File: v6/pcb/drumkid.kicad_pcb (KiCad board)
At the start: 2 copper layers, 90 x 140 mm, 52 parts, among them J1 DIN-5_180degree, J2 DIN-5_180degree, J3 Conn_01x15, J4 Conn_01x15, J9 AudioJack3_Ground_Switch, SW1 SW_Push, SW2 SW_Push, SW3 SW_Push, SW4 SW_Push, SW5 SW_Push, SW6 SW_Push, SW7 SW_SPDT, SW8 SW_SPDT, U1 6N138

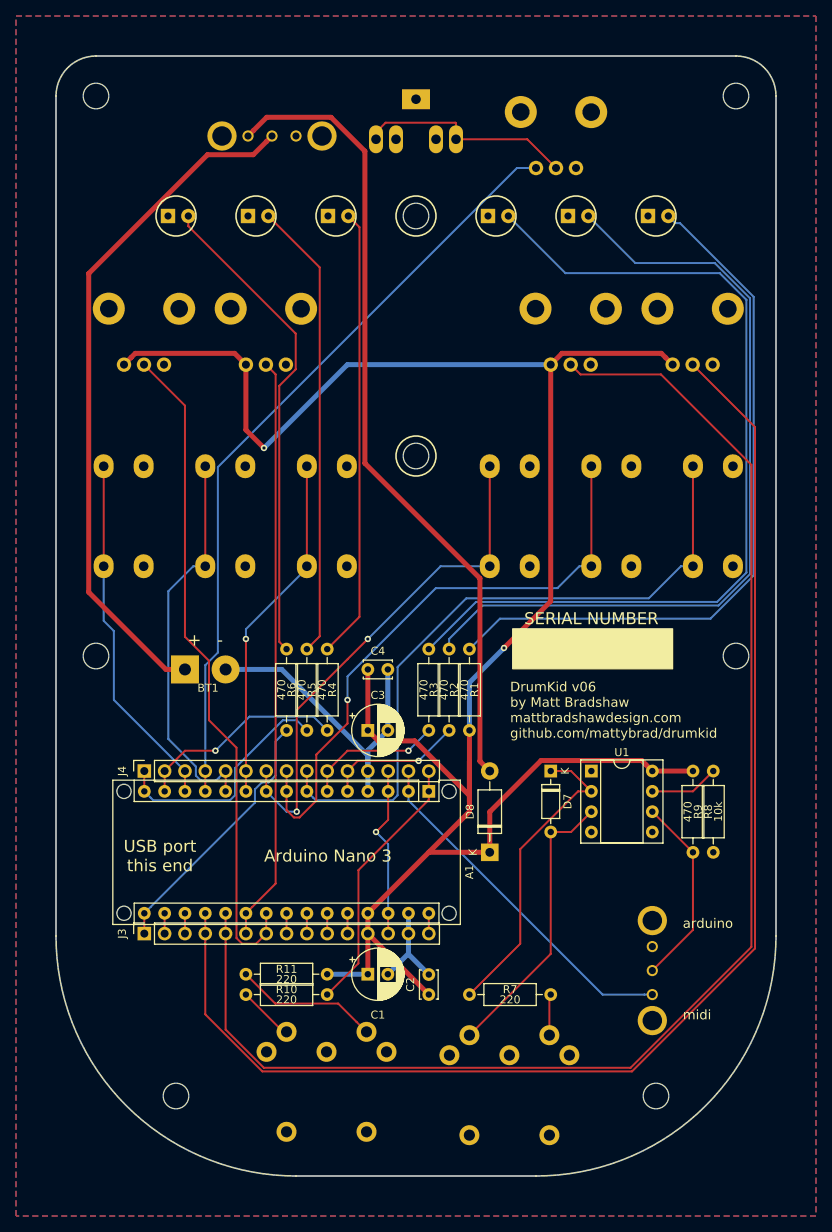
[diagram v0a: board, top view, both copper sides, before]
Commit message: added mounting holes
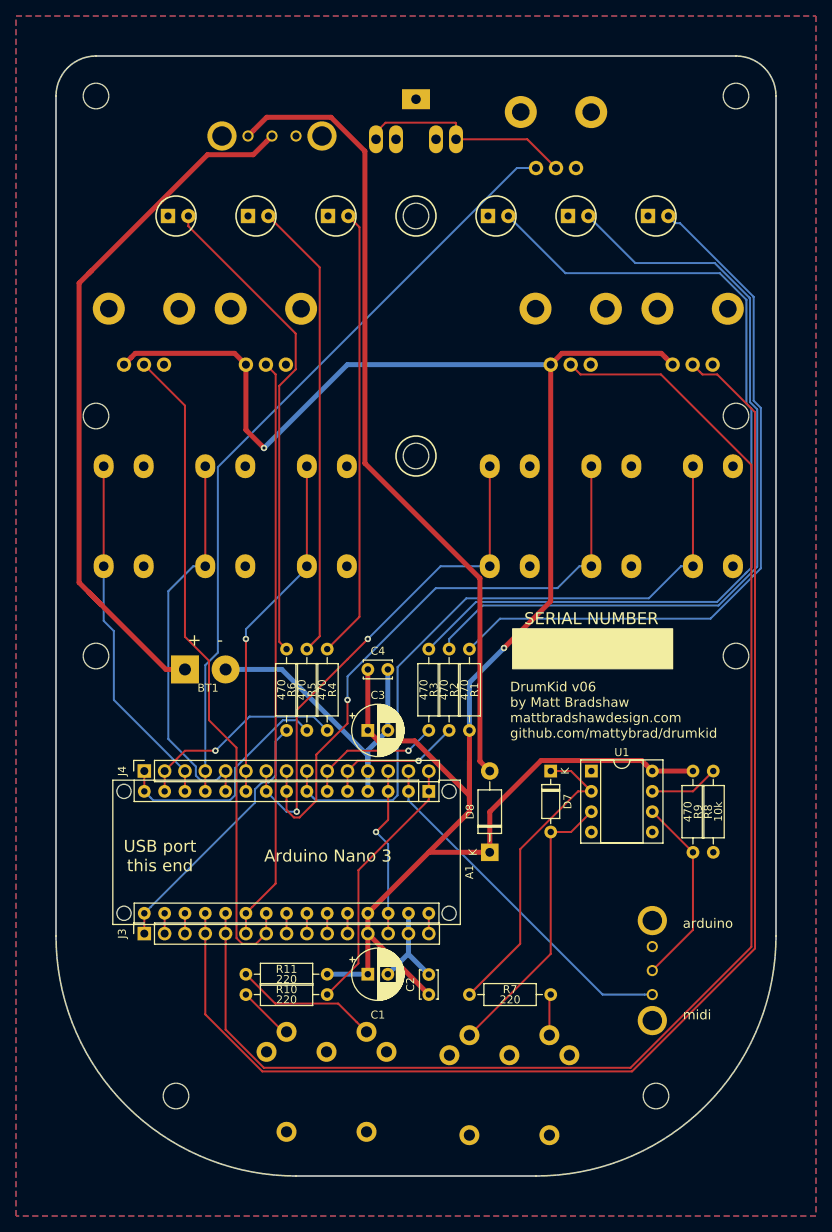
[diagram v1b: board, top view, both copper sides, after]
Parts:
- added H10: MountingHole, drumkidcustom:MountingHole_3.2mm_M3, B.Cu at (140.0, 75.0)
- added H9: MountingHole, drumkidcustom:MountingHole_3.2mm_M3, B.Cu at (60.0, 75.0)
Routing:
- net Net-(BT1-Pad1): track 85.9 -> 89.5 mm
- net /ANALOG_0: track 166.9 -> 168.0 mm
- net Net-(D2-Pad2): track 101.2 -> 102.1 mm
- net Net-(D1-Pad2): track 89.0 -> 89.8 mm
- net Net-(D3-Pad2): track 111.9 -> 112.5 mm
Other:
- board text added: "chance pitch note beat"
- board text added: "midpoint drop drone gremlin"
- board text added: "range crop modulate beats/bar"
- board text added: "zoom crush tuning tempo"
- board text removed: "chance pitch slop beat"

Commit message: finalised parameter labels on pcb
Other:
- board text added: "chance pitch drone beat"
- board text added: "midpoint drop note tempo"
- board text added: "range crop tuning swing"
- board text added: "zoom crush modulate beats/bar"
- board text removed: "chance pitch note beat"
- board text removed: "midpoint drop drone gremlin"
- board text removed: "range crop modulate beats/bar"
- board text removed: "zoom crush tuning tempo"
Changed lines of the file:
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@@
   (gr_line (start 144.9324 71.1708) (end 54.991 71.1708) (layer B.SilkS) (width 0.1))
   (gr_line (start 144.9324 73.279) (end 54.9656 73.279) (layer B.SilkS) (width 0.1))
-  (gr_text "midpoint\ndrop\ndrone\ngremlin" (at 66.04 73.66) (layer B.SilkS)
+  (gr_text "midpoint\ndrop\nnote\ntempo" (at 66.04 73.66) (layer B.SilkS)
     (effects (font (size 1.2 1.2) (thickness 0.3)) (justify mirror))
   )
-  (gr_text "range\ncrop\nmodulate\nbeats/bar" (at 81.28 73.66) (layer B.SilkS)
+  (gr_text "range\ncrop\ntuning\nswing" (at 81.28 73.66) (layer B.SilkS)
     (effects (font (size 1.2 1.2) (thickness 0.3)) (justify mirror))
   )
-  (gr_text "zoom\ncrush\ntuning\ntempo" (at 119.38 73.66) (layer B.SilkS)
+  (gr_text "zoom\ncrush\nmodulate\nbeats/bar" (at 119.38 73.66) (layer B.SilkS)
     (effects (font (size 1.2 1.2) (thickness 0.3)) (justify mirror))
   )
-  (gr_text "chance\npitch\nnote\nbeat" (at 134.62 73.66) (layer B.SilkS)
+  (gr_text "chance\npitch\ndrone\nbeat" (at 134.62 73.66) (layer B.SilkS)
     (effects (font (size 1.2 1.2) (thickness 0.3)) (justify mirror))
   )

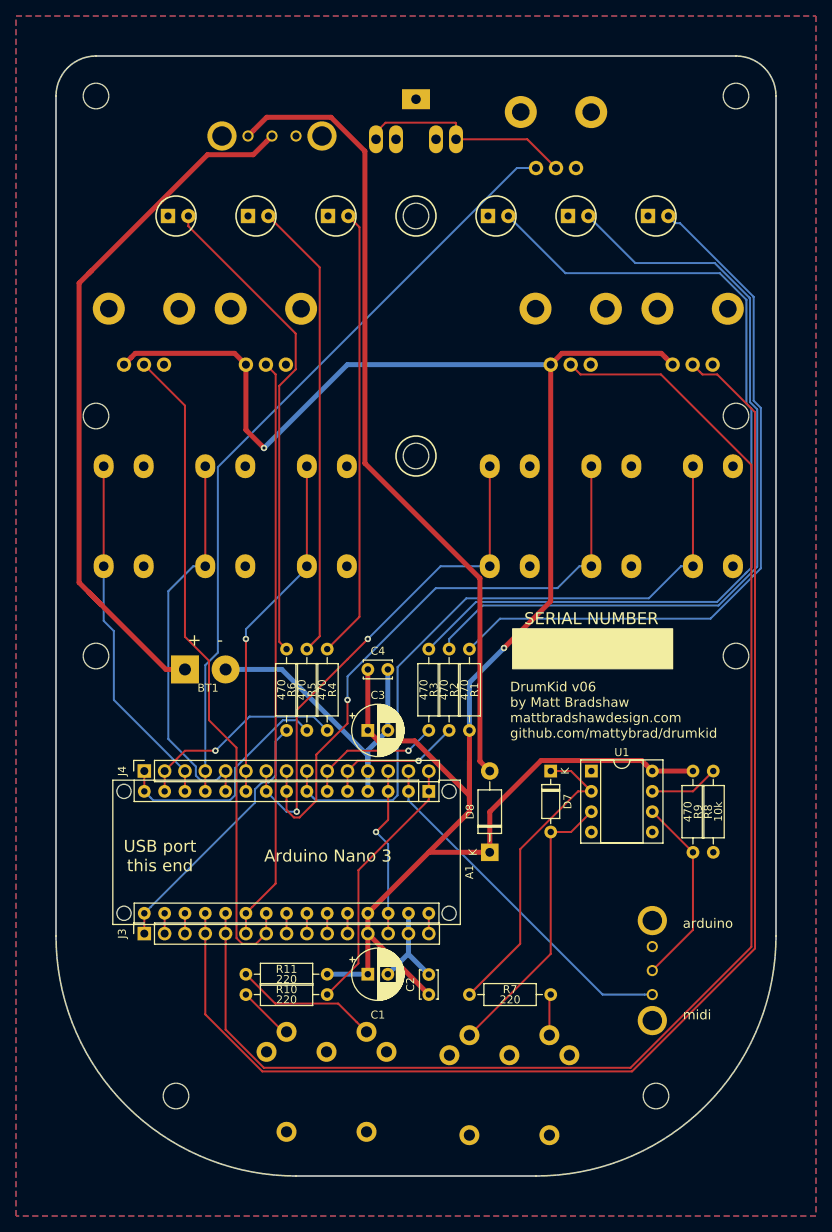
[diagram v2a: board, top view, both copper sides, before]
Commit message: drumkid v6 prototype pcb ordered!
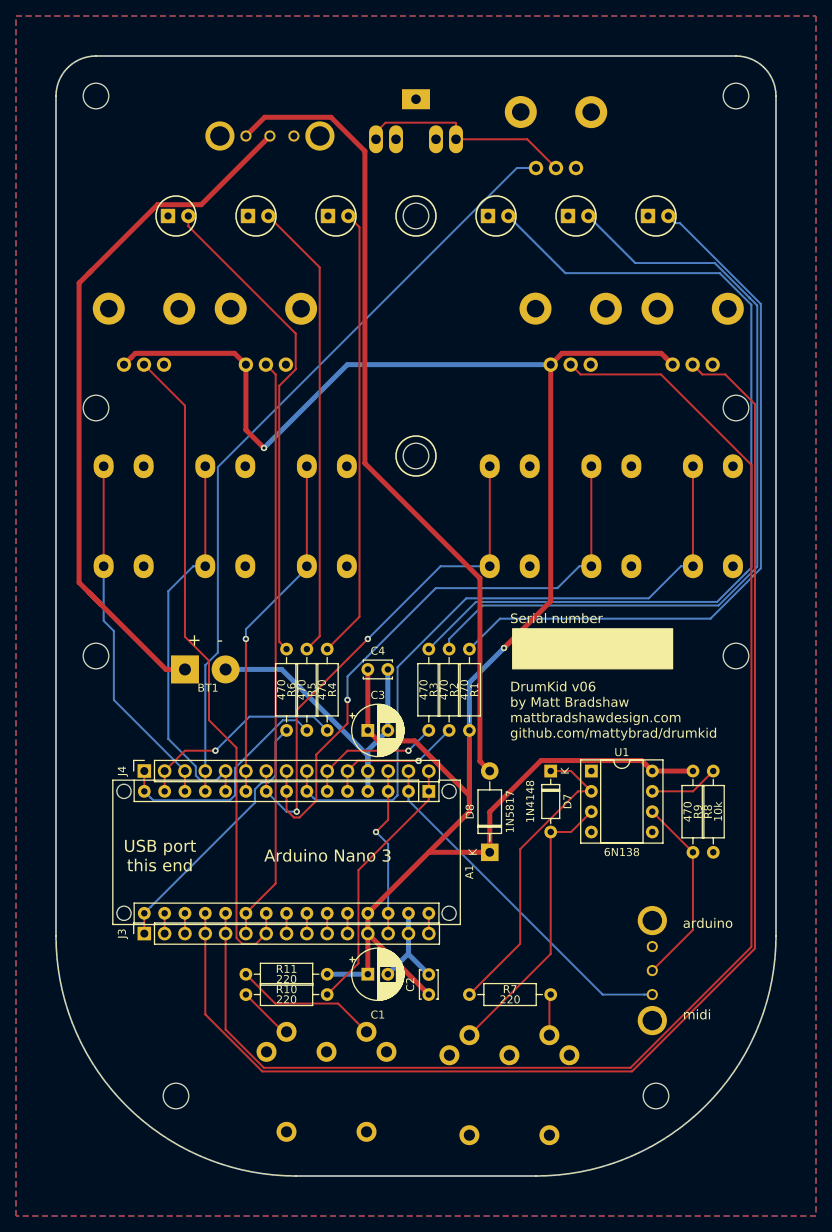
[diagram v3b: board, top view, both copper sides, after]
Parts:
- SW7: moved to B.Cu
- moved SW7 6.26 mm to (78.7, 40.0), turned to 0 degrees
- moved H10 1.00 mm to (140.0, 74.0)
- moved H9 1.00 mm to (60.0, 74.0)
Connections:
- SW7 pad 1: Net-(SW7-Pad1) -> Net-(D8-Pad2)
- SW7 pad 3: Net-(D8-Pad2) -> Net-(SW7-Pad3)
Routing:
- net /ANALOG_0: track 168.0 -> 168.5 mm
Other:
- board text added: "1N4148"
- board text added: "1N5817"
- board text added: "6N138"
- board text added: "Serial number"
- board text removed: "SERIAL NUMBER"
